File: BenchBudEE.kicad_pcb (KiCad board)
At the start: 4 copper layers, 165.1 x 63.5 mm, 123 parts, among them K1 1461069-5, P1 24-pin Mini-Fit Jr., P2 CONN_2, P3 CONN_3X2, P4 12-pin Terminal Block, P5 3-pin TB, Q1 2N3404, Q2 DMN65D8L-7, Q3 AOD476, Q4 AOD476, SW1 Power Switch, U1 LTV-816S, U10 LMT84, U11 OPA4170, U2 AP5726, U3 LM317T, U4 LM317T, U5 LM337T, U6 LM337T, U8 MCP4801, U9 MCP3901

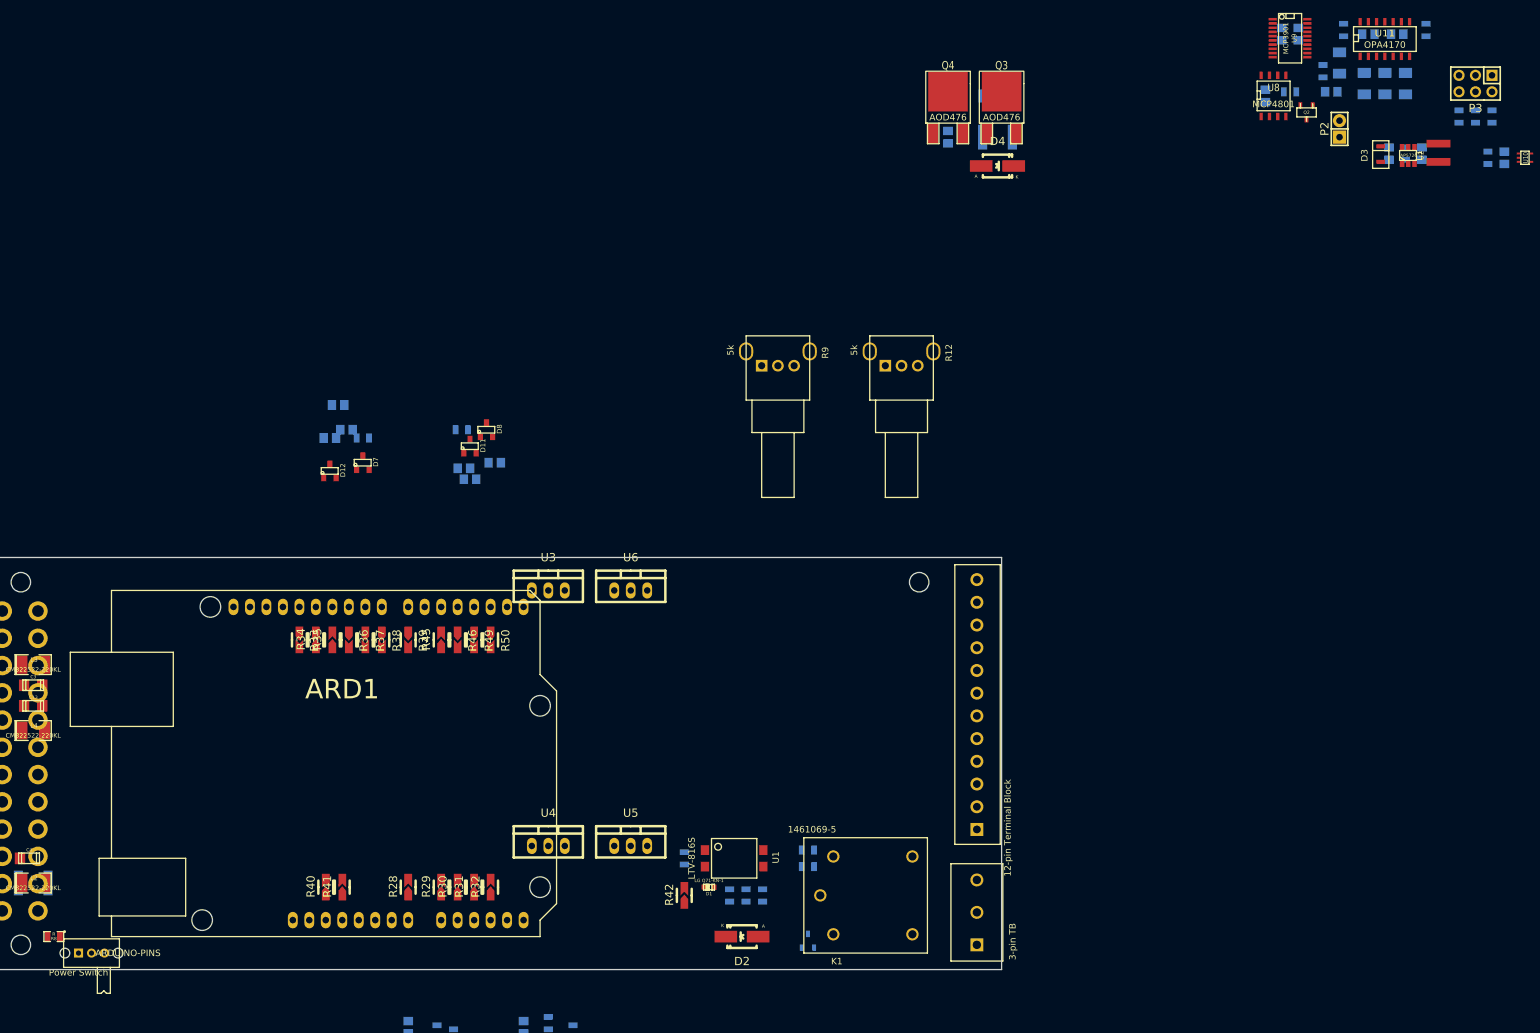
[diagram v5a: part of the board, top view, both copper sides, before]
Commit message: Updates from Layout Work Session 3 video
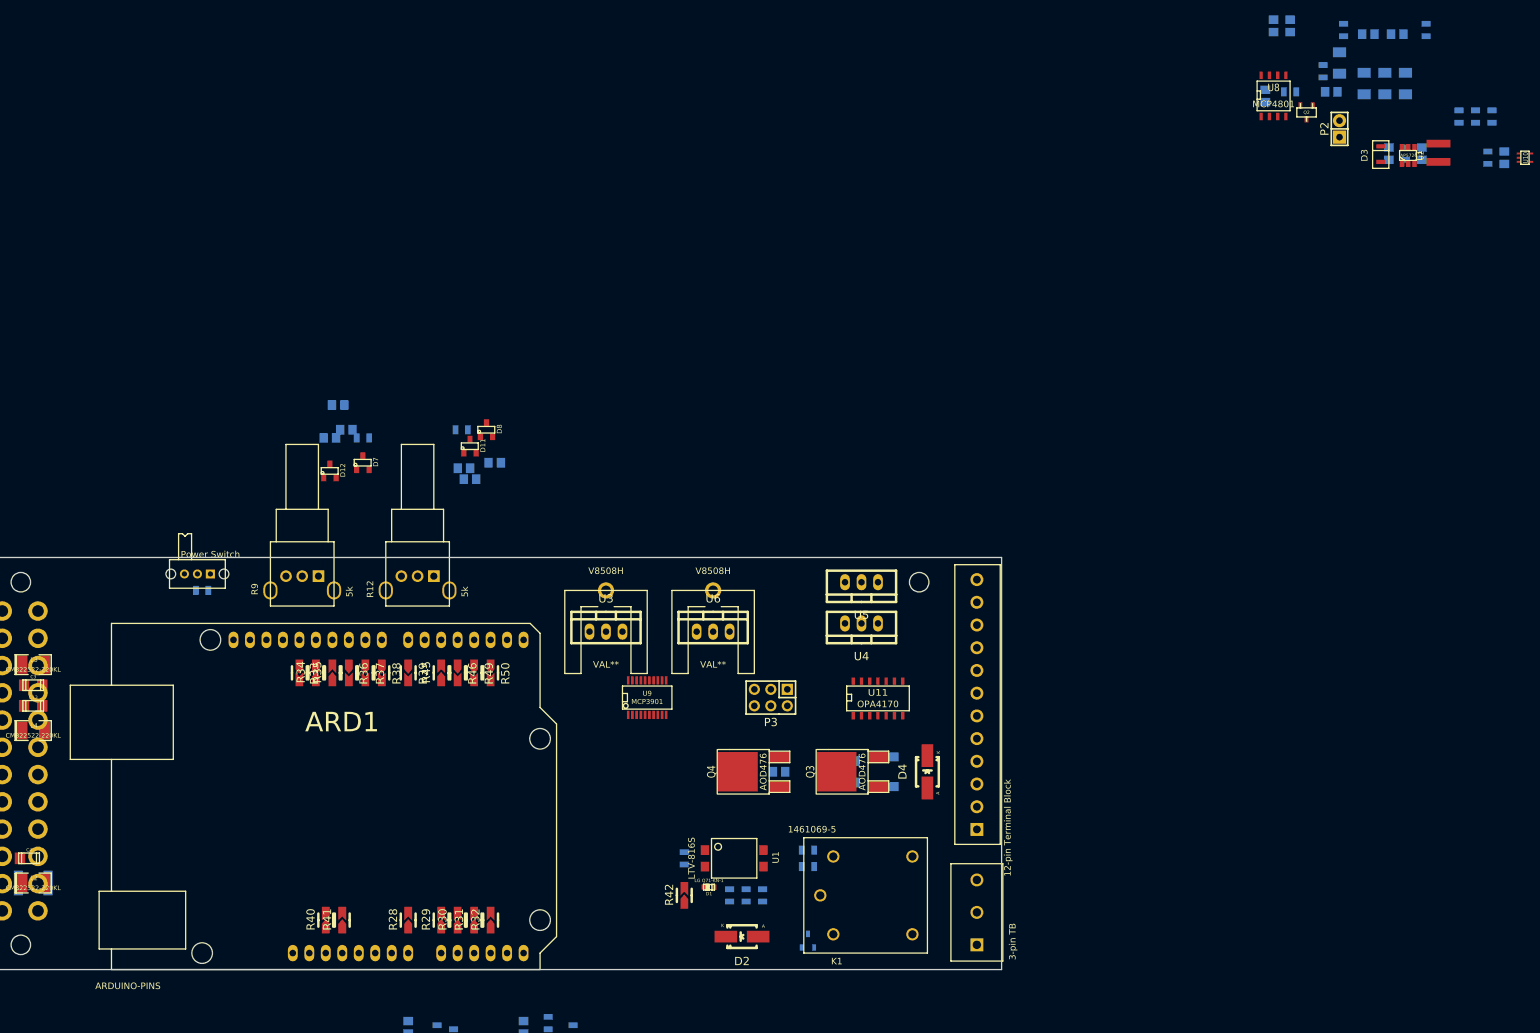
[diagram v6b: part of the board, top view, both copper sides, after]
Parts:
- added V8508H: VAL**, BenchBudEE:V8508H, F.Cu at (175.3, 55.9)
- added V8508H: VAL**, BenchBudEE:V8508H, F.Cu at (191.8, 55.9)
- R8: moved to B.Cu
- moved P3 144.0 mm to (200.7, 72.4)
- moved U9 141.9 mm to (181.6, 72.4), turned to 0 degrees
- moved U11 128.2 mm to (217.2, 72.4)
- moved R20 105.8 mm to (213.4, 83.8), turned to 90 degrees
- moved Q4 101.8 mm to (201.9, 83.8), turned to 90 degrees
- moved C12 101.2 mm to (201.9, 83.8), turned to 180 degrees
- moved Q3 100.3 mm to (217.2, 83.8), turned to 90 degrees
- moved TH5 99.3 mm to (218.4, 83.8), turned to 90 degrees
- moved D4 94.0 mm to (224.8, 83.8), turned to 90 degrees
- moved R12 74.5 mm to (151.1, 55.9), turned to 90 degrees
- moved R9 73.4 mm to (133.3, 55.9), turned to 90 degrees
- moved SW1 61.9 mm to (114.3, 53.3), turned to 180 degrees
- moved U4 59.2 mm to (214.6, 61.0), turned to 180 degrees
- moved R8 58.0 mm to (113.0, 55.9)
- moved U5 54.0 mm to (214.6, 54.6), turned to 180 degrees
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
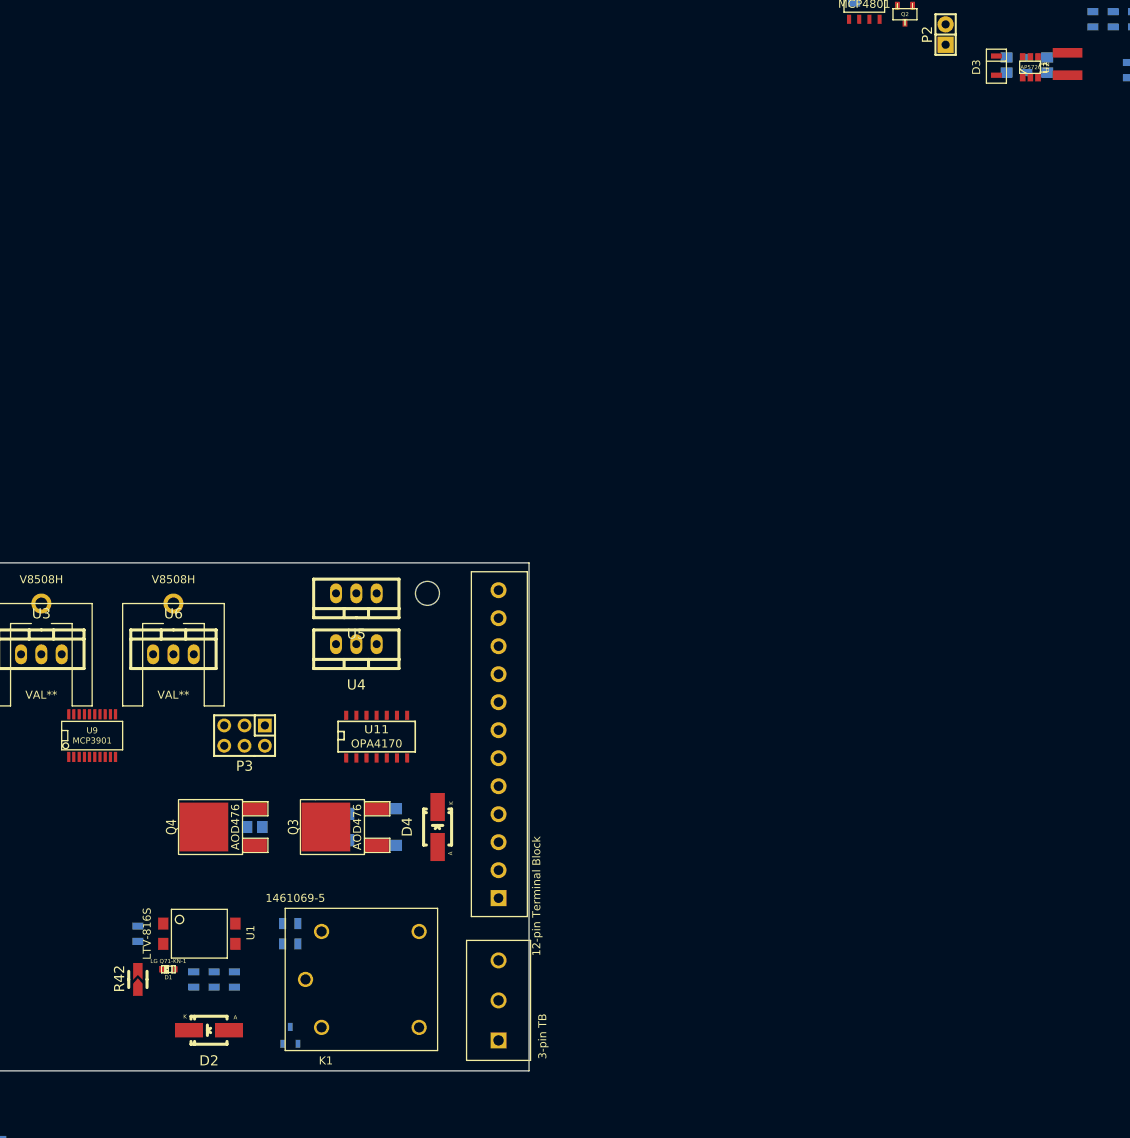
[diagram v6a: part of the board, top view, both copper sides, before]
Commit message: Updates from Layout Work Session 4 video
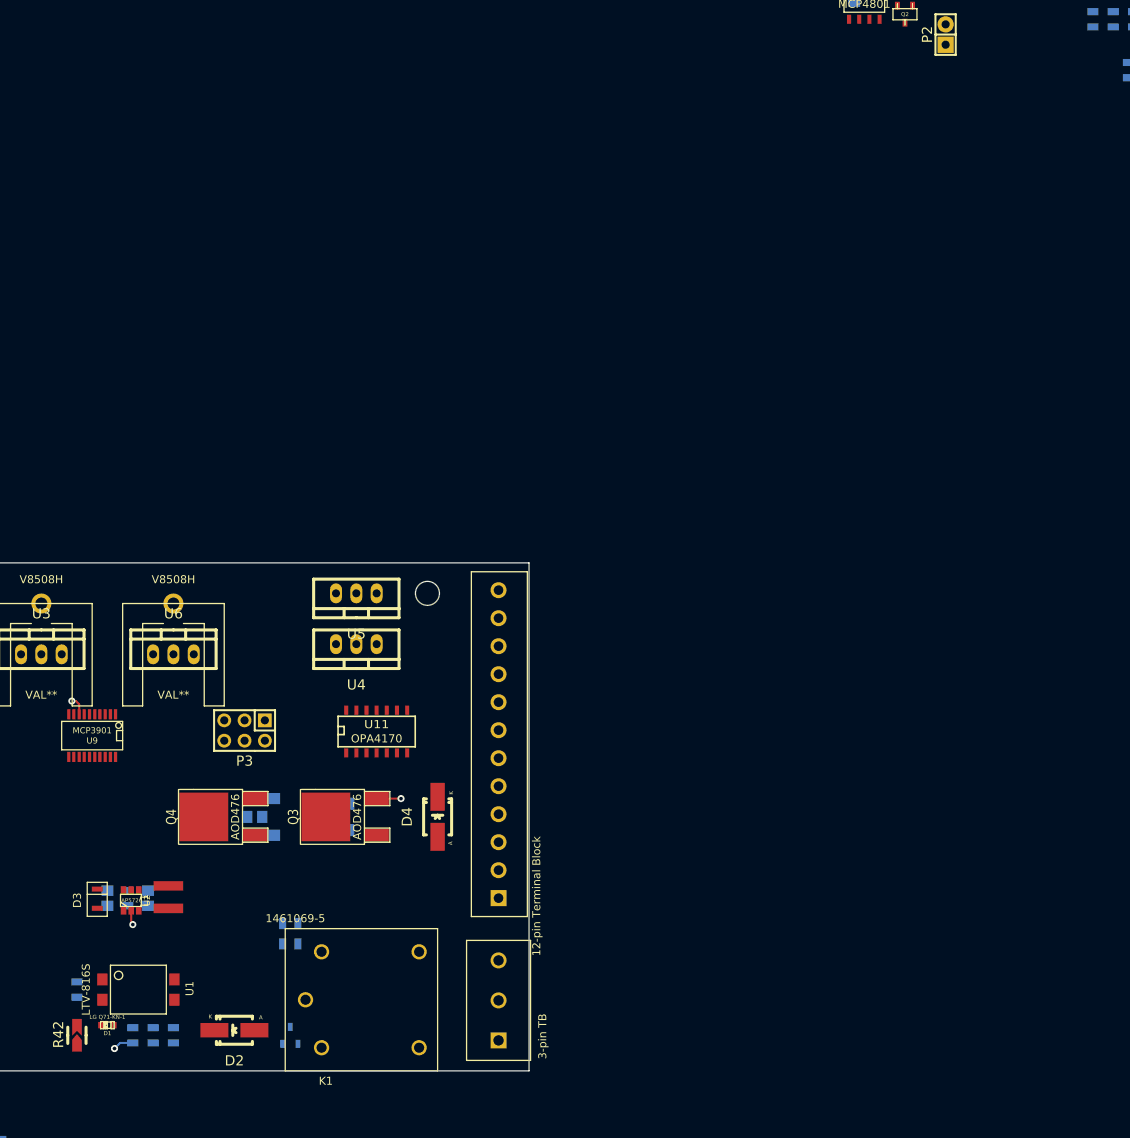
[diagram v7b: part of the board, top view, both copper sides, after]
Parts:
- moved C2 153.2 mm to (183.5, 92.7)
- moved U2 153.2 mm to (186.5, 93.0)
- moved C1 153.2 mm to (188.6, 92.7)
- moved D3 153.2 mm to (182.2, 94.0)
- moved L1 153.2 mm to (191.1, 94.0)
- moved R7 153.2 mm to (186.1, 92.7)
- moved TH5 15.3 mm to (203.2, 82.5)
- moved D1 10.3 mm to (183.5, 108.6)
- moved R2 10.3 mm to (186.7, 109.9)
- moved R6 10.3 mm to (189.2, 109.9)
- moved U1 10.3 mm to (182.9, 102.9)
- moved R1 10.3 mm to (179.7, 104.1)
- moved R3 10.3 mm to (191.8, 109.9)
- moved R42 10.3 mm to (179.7, 109.9)
- moved D2 3.17 mm to (199.4, 109.2)
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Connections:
- C1 pad 2: GND -> GND_LED
- C10 pad 2: Net-(C10-Pad2) -> GND_TC
- C12 pad 1: GND -> GND_FAN
- C14 pad 1: AGND -> GND_TC
- C15 pad 2: AGND -> GND_PWR
- C16 pad 2: AGND -> GND_TC
- C17 pad 1: AGND -> GND_PWR
- C18 pad 1: AGND -> GND_TC
- C19 pad 2: AGND -> GND_TC
- C2 pad 2: GND -> GND_LED
- C20 pad 2: AGND -> GND_PWR
- C21 pad 1: AGND -> GND_PWR
- C22 pad 1: AGND -> GND_TC
- C23 pad 2: AGND -> GND_TC
- C24 pad 2: AGND -> GND_PWR
- C25 pad 1: AGND -> GND_PWR
- C5 pad 1: AGND -> GND_TC
- C6 pad 1: AGND -> GND_TC
- C8 pad 1: AGND -> GND_TC
- C9 pad 1: AGND -> GND_TC
- D11 pad 2: Net-(C21-Pad2) -> Net-(D11-Pad2)
- P4 pad 10: /Fan/TACH_IN -> +5V
- P4 pad 11: /Fan/FAN_OUT- -> /PowerAdjustmentMonitor/V-_ADJ
- P4 pad 12: /Fan/FAN_OUT+ -> /PowerAdjustmentMonitor/V+_ADJ
- P4 pad 3: GND -> /Fan/TACH_IN
- P4 pad 4: /PowerAdjustmentMonitor/V+_ADJ -> /Fan/FAN_OUT-
- P4 pad 5: /PowerAdjustmentMonitor/V-_ADJ -> /Fan/FAN_OUT+
- P4 pad 6: +3.3V -> /TerminalBlock/TC_IN-
- P4 pad 7: +5V -> /TerminalBlock/TC_IN+
- P4 pad 8: /TerminalBlock/TC_IN+ -> GND
- P4 pad 9: /TerminalBlock/TC_IN- -> +3.3V
- Q2 pad 3: AGND -> GND_FAN
- Q3 pad 3: GND -> GND_FAN
- R12 pad 1: AGND -> GND_PWR
- R16 pad 1: AGND -> GND_PWR
- R17 pad 1: AGND -> GND_PWR
- R2 pad 1: GND -> GND_RELAY
- R20 pad 2: GND -> GND_FAN
- R22 pad 1: AGND -> GND_TC
- R47 pad 1: Net-(C10-Pad2) -> GND_TC
- R48 pad 1: AGND -> GND_TC
- R52 pad 1: AGND -> GND_TC
- R53 pad 1: AGND -> GND_TC
- R6 pad 1: GND -> GND_RELAY
- R7 pad 2: GND -> GND_LED
- R9 pad 2: AGND -> GND_PWR
- U10 pad 1: Net-(C10-Pad2) -> GND_TC
- U10 pad 2: Net-(C10-Pad2) -> GND_TC
- U10 pad 5: Net-(C10-Pad2) -> GND_TC
- U2 pad 2: GND -> GND_LED
- U8 pad 7: AGND -> GND_FAN
- U9 pad 11: AGND -> GND_TC
- U9 pad 8: AGND -> GND_TC
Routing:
- net GND_FAN: track 0.00 -> 3.05 mm, vias 0 -> 1
- net GND_RELAY: track 0.00 -> 2.58 mm, vias 0 -> 1
- net GND_TC: track 0.00 -> 2.33 mm, vias 0 -> 1
- net GND_LED: track 0.00 -> 1.83 mm, vias 0 -> 1
- added copper zone on GND, net GND_FAN
- added copper zone on GND, net GND_LED
- added copper zone on GND, net GND_PWR
- added copper zone on GND, net GND_RELAY
- added copper zone on GND, net GND_TC

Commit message: Updates from Layout Work Session 5 video
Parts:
- added TP1: CONN_1, Connect:1pin, F.Cu at (108.6, 87.6)
- moved U8 140.6 mm to (181.6, 81.9)
- moved C10 62.9 mm to (275.0, 38.7)
- moved C11 62.9 mm to (238.1, 29.2)
- moved C5 62.9 mm to (241.9, 18.4)
- moved C8 62.9 mm to (254.0, 19.7)
- moved C9 62.9 mm to (258.4, 19.7)
- moved P2 62.9 mm to (249.6, 34.3)
- moved R19 62.9 mm to (241.9, 28.6)
- moved R21 62.9 mm to (253.4, 27.3)
- moved R22 62.9 mm to (249.6, 24.1)
- moved R23 62.9 mm to (259.7, 27.3)
- moved R25 62.9 mm to (262.9, 19.1)
- moved R27 62.9 mm to (250.2, 19.1)
- moved R43 62.9 mm to (270.5, 32.4)
- moved R44 62.9 mm to (273.1, 32.4)
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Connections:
- C10 pad 2: GND_TC -> AGND
- C12 pad 1: GND_FAN -> AGND
- C14 pad 1: GND_TC -> AGND
- C16 pad 2: GND_TC -> AGND
- C18 pad 1: GND_TC -> AGND
- C19 pad 2: GND_TC -> AGND
- C22 pad 1: GND_TC -> AGND
- C23 pad 2: GND_TC -> AGND
- C5 pad 1: GND_TC -> AGND
- C6 pad 1: GND_TC -> AGND
- C8 pad 1: GND_TC -> AGND
- C9 pad 1: GND_TC -> AGND
- P4 pad 8: GND -> GND_PWR
- Q2 pad 3: GND_FAN -> AGND
- Q3 pad 3: GND_FAN -> AGND
- R20 pad 2: GND_FAN -> AGND
- R47 pad 1: GND_TC -> AGND
- R52 pad 1: GND_TC -> AGND
- R53 pad 1: GND_TC -> AGND
- U10 pad 1: GND_TC -> AGND
- U10 pad 2: GND_TC -> AGND
- U10 pad 5: GND_TC -> AGND
- U8 pad 7: GND_FAN -> AGND
- U9 pad 11: GND_TC -> AGND
- U9 pad 8: GND_TC -> AGND
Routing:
- net +12V: track 0.00 -> 208.8 mm, vias 0 -> 1
- net -12V: track 0.00 -> 206.7 mm, vias 0 -> 1
- net +12C: track 0.00 -> 188.2 mm, vias 0 -> 2
- net /Relay/RELAY_COM: track 0.00 -> 24.2 mm
- net /Relay/RELAY_NC: track 0.00 -> 10.4 mm
- net /Relay/RELAY_NO: track 0.00 -> 10.3 mm
- net AGND: track 0.00 -> 5.38 mm, vias 0 -> 2
- net GND_FAN: track 3.05 -> 0.00 mm, vias 1 -> 0
- net GND_TC: track 2.33 -> 0.00 mm, vias 1 -> 0
- net +5P: track 0.00 -> 2.24 mm, vias 0 -> 1
- net +12P: track 0.00 -> 2.16 mm, vias 0 -> 1
- net +5V: track 0.00 -> 1.76 mm, vias 0 -> 1
- added copper zone on PWR, net +12P
- added copper zone on PWR, net +5P
- added copper zone on PWR, net +5V
- added copper zone on GND, net AGND
- removed copper zone on GND, net GND_FAN
- removed copper zone on GND, net GND_TC
